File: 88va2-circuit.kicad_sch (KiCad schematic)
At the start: 0 parts

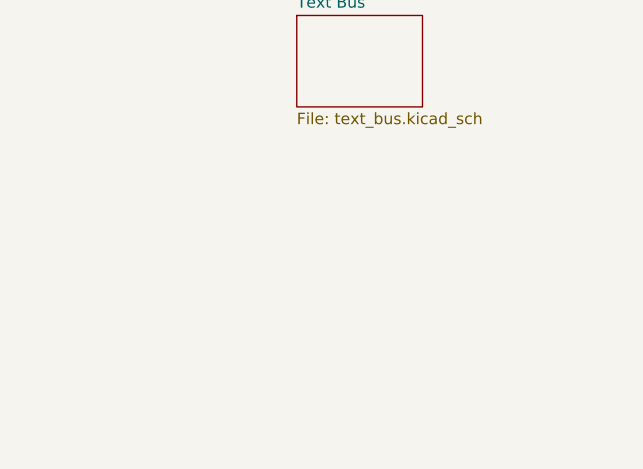
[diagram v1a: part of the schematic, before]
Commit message: add IC13 to schematic
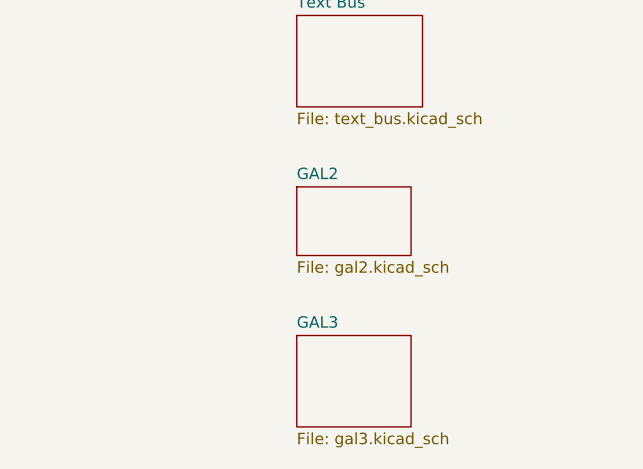
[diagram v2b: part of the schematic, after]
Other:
- added sheet GAL2 (gal2.kicad_sch)
- added sheet GAL3 (gal3.kicad_sch)
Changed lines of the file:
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@@
+    )
+  )
+  (sheet (at 127 143.51) (size 12.7 10.16) (fields_autoplaced)
+    (stroke (width 0.1524) (type solid))
+    (fill (color 0 0 0 0.0000))
+    (property "Sheetname" "GAL3" (at 127 142.7984 0)
+      (effects (font (size 1.27 1.27)) (justify left bottom))
+    )
+    (property "Sheetfile" "gal3.kicad_sch" (at 127 154.2546 0)
+      (effects (font (size 1.27 1.27)) (justify left top))
+    )
+    (instances
+      (project "88va2-circuit"
+        (path "/8cd193ae-a369-4130-9ba4-f2075fa60e2b" (page "7"))
+      )
     )
   )
@@
       )
     )
+  )
+  (sheet (at 127 127) (size 12.7 7.62) (fields_autoplaced)
+    (stroke (width 0.1524) (type solid))
+    (fill (color 0 0 0 0.0000))
+    (property "Sheetname" "GAL2" (at 127 126.2884 0)
+      (effects (font (size 1.27 1.27)) (justify left bottom))
+    )
+    (property "Sheetfile" "gal2.kicad_sch" (at 127 135.2046 0)
+      (effects (font (size 1.27 1.27)) (justify left top))
+    )
+    (instances
+      (project "88va2-circuit"
+        (path "/8cd193ae-a369-4130-9ba4-f2075fa60e2b" (page "6"))
+      )
+    )

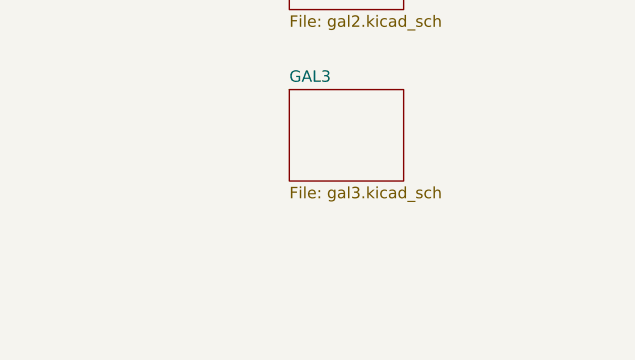
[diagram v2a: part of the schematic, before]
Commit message: add GVRAM
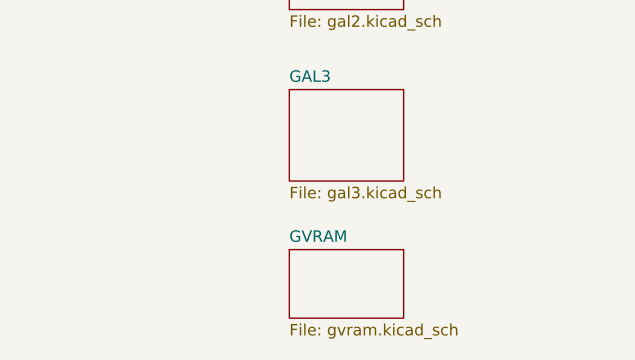
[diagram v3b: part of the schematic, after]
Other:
- added sheet GVRAM (gvram.kicad_sch)
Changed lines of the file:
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@@
+    )
+  )
+  (sheet (at 127 161.29) (size 12.7 7.62) (fields_autoplaced)
+    (stroke (width 0.1524) (type solid))
+    (fill (color 0 0 0 0.0000))
+    (property "Sheetname" "GVRAM" (at 127 160.5784 0)
+      (effects (font (size 1.27 1.27)) (justify left bottom))
+    )
+    (property "Sheetfile" "gvram.kicad_sch" (at 127 169.4946 0)
+      (effects (font (size 1.27 1.27)) (justify left top))
+    )
+    (instances
+      (project "88va2-circuit"
+        (path "/8cd193ae-a369-4130-9ba4-f2075fa60e2b" (page "8"))
+      )
     )
   )

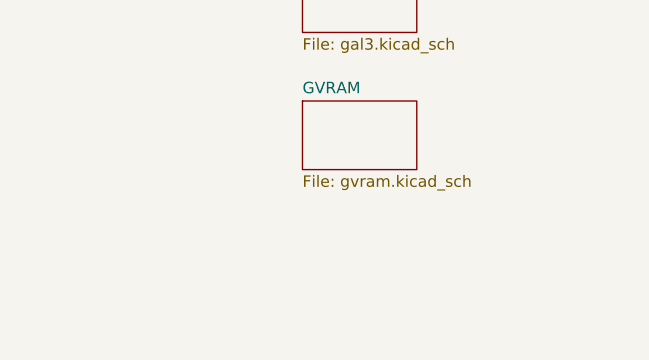
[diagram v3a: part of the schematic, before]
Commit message: schematic: add IC22, IC6
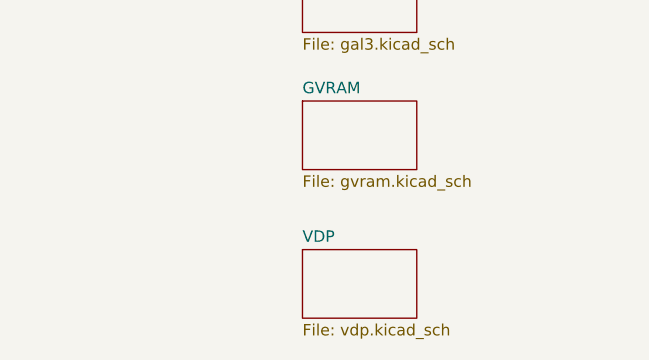
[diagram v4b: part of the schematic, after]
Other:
- added sheet VDP (vdp.kicad_sch)
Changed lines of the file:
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@@
+    )
+  )
+  (sheet (at 127 177.8) (size 12.7 7.62) (fields_autoplaced)
+    (stroke (width 0.1524) (type solid))
+    (fill (color 0 0 0 0.0000))
+    (property "Sheetname" "VDP" (at 127 177.0884 0)
+      (effects (font (size 1.27 1.27)) (justify left bottom))
+    )
+    (property "Sheetfile" "vdp.kicad_sch" (at 127 186.0046 0)
+      (effects (font (size 1.27 1.27)) (justify left top))
+    )
+    (instances
+      (project "88va2-circuit"
+        (path "/8cd193ae-a369-4130-9ba4-f2075fa60e2b" (page "9"))
+      )
     )
   )

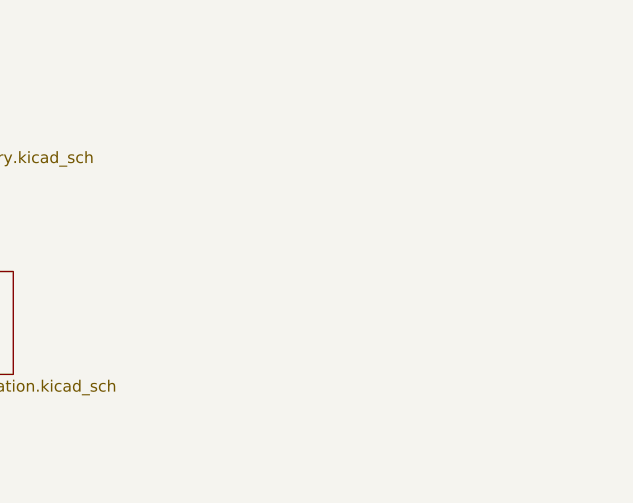
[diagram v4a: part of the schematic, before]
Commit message: add display clock generator
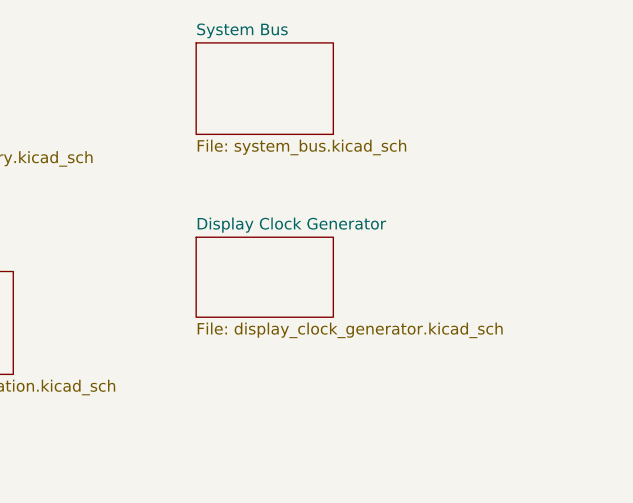
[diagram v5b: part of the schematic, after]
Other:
- added sheet Display Clock Generator (display_clock_generator.kicad_sch)
- added sheet System Bus (system_bus.kicad_sch)
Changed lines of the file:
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@@
+    )
+  )
+  (sheet (at 162.56 33.02) (size 15.24 10.16) (fields_autoplaced)
+    (stroke (width 0.1524) (type solid))
+    (fill (color 0 0 0 0.0000))
+    (property "Sheetname" "System Bus" (at 162.56 32.3084 0)
+      (effects (font (size 1.27 1.27)) (justify left bottom))
+    )
+    (property "Sheetfile" "system_bus.kicad_sch" (at 162.56 43.7646 0)
+      (effects (font (size 1.27 1.27)) (justify left top))
+    )
+    (instances
+      (project "88va2-circuit"
+        (path "/8cd193ae-a369-4130-9ba4-f2075fa60e2b" (page "10"))
+      )
     )
   )
@@
       )
     )
+  )
+  (sheet (at 162.56 54.61) (size 15.24 8.89) (fields_autoplaced)
+    (stroke (width 0.1524) (type solid))
+    (fill (color 0 0 0 0.0000))
+    (property "Sheetname" "Display Clock Generator" (at 162.56 53.8984 0)
+      (effects (font (size 1.27 1.27)) (justify left bottom))
+    )
+    (property "Sheetfile" "display_clock_generator.kicad_sch" (at 162.56 64.0846 0)
+      (effects (font (size 1.27 1.27)) (justify left top))
+    )
+    (instances
+      (project "88va2-circuit"
+        (path "/8cd193ae-a369-4130-9ba4-f2075fa60e2b" (page "11"))
+      )
+    )
